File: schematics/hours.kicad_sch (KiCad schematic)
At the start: 53 parts, among them U27 74HC04, U28 74HC157, U29 74HC157, U30 74HC138, U32 74HC139

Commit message: 24-12 converter cleanup
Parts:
- removed D28, D29, D30, D31, D32, D33, D34, D35, D36: 1N4148, Diode_THT:D_DO-35_SOD27_P7.62mm_Horizontal, symbol Diode:1N4148
- removed R44: 1K, Package_DIP:DIP-16_W7.62mm, symbol Device:R
- removed R45, R46, R47: 10K, Package_DIP:DIP-16_W7.62mm, symbol Device:R
- removed unit 1 of U27
- added D46, D48, D53, D62: 1N4148, Diode_THT:D_DO-35_SOD27_P7.62mm_Horizontal, symbol Diode:1N4148
- added R53, R54: 4K7, Package_DIP:DIP-16_W7.62mm, symbol Device:R
- added U31: 74HC04, symbol 74xx:74HC04
- R48, R49, R50, R51, R52: value 10K -> 4K7
- U28, U29: value 74HC157 -> 74HC257
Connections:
- net +3V3: now also U29.3 (1B); no longer U30.6 (G1)
- net GND: now also U27.11, U28.15 (~{G}), U28.2 (1A), R53.2, R54.2; no longer U27.13, U30.5 (~{G}2B)
- net HI2: now also U27.13, D46.2 (A)
- net HI3: now also U30.4 (~{G}2A), D53.2 (A)
- net HI4: now also D48.2 (A)
- net HI5: now also U30.5 (~{G}2B), D62.2 (A)
- net at D37.2 (A), D45.2 (A), D47.2 (A)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: no longer U27.11
- net at U32.15 (2~{G}): now also U31.2
- net at U32.1 (1~{G}): now also U27.12, U30.6 (G1)
- net at U32.13 (2B): now also D46.1 (K), D48.1 (K), R53.1
- net at U27.10: no longer U29.3 (1B)
- new net: D53.1 (K), D62.1 (K), R54.1, U31.1
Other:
- note added: "12/24 mode switch"
- note added: "24 hour time in BCD"
- note added: "If leading digit is 0, setting upper bits 3 and 4 to '1' blanks instead of displaying it."
- note added: "Sets segment C of LED to make it "A" instead of "P"."
- note added: "always the same"
- moved on the sheet: C26, C27, C28, C29, C30, D37, D38, D41, D43, D45, D47, D49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

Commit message: added some PCB footprints
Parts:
- C20: renamed from C26; footprint Package_SO:SOIC-8_3.9x4.9mm_P1.27mm -> Capacitor_THT:C_Disc_D5.1mm_W3.2mm_P5.00mm
- C21: renamed from C27; footprint Package_SO:SOIC-8_3.9x4.9mm_P1.27mm -> Capacitor_THT:C_Disc_D5.1mm_W3.2mm_P5.00mm
- C22: renamed from C28; footprint Package_SO:SOIC-8_3.9x4.9mm_P1.27mm -> Capacitor_THT:C_Disc_D5.1mm_W3.2mm_P5.00mm
- C23: renamed from C29; footprint Package_SO:SOIC-8_3.9x4.9mm_P1.27mm -> Capacitor_THT:C_Disc_D5.1mm_W3.2mm_P5.00mm
- C24: renamed from C30; footprint Package_SO:SOIC-8_3.9x4.9mm_P1.27mm -> Capacitor_THT:C_Disc_D5.1mm_W3.2mm_P5.00mm
- R22: renamed from R53; footprint Package_DIP:DIP-16_W7.62mm -> Resistor_THT:R_Axial_DIN0207_L6.3mm_D2.5mm_P10.16mm_Horizontal
- R23: renamed from R54; footprint Package_DIP:DIP-16_W7.62mm -> Resistor_THT:R_Axial_DIN0207_L6.3mm_D2.5mm_P10.16mm_Horizontal
- R24: renamed from R52; footprint Package_DIP:DIP-16_W7.62mm -> Resistor_THT:R_Axial_DIN0207_L6.3mm_D2.5mm_P10.16mm_Horizontal
- R25: renamed from R48; footprint Package_DIP:DIP-16_W7.62mm -> Resistor_THT:R_Axial_DIN0207_L6.3mm_D2.5mm_P10.16mm_Horizontal
- R26: renamed from R49; footprint Package_DIP:DIP-16_W7.62mm -> Resistor_THT:R_Axial_DIN0207_L6.3mm_D2.5mm_P10.16mm_Horizontal
- R27: renamed from R50; footprint Package_DIP:DIP-16_W7.62mm -> Resistor_THT:R_Axial_DIN0207_L6.3mm_D2.5mm_P10.16mm_Horizontal
- R28: renamed from R51; footprint Package_DIP:DIP-16_W7.62mm -> Resistor_THT:R_Axial_DIN0207_L6.3mm_D2.5mm_P10.16mm_Horizontal
- U11: renamed from U27; footprint (none) -> Package_DIP:DIP-14_W7.62mm
- U11: renamed from U31; footprint (none) -> Package_DIP:DIP-14_W7.62mm
- U13: renamed from U30; footprint Package_TO_SOT_SMD:SOT-23-5 -> Package_DIP:DIP-16_W7.62mm
- U14: renamed from U28; footprint Filter:Filter_1411-5_1.4x1.1mm -> Package_DIP:DIP-16_W7.62mm
- U15: renamed from U29; footprint Filter:Filter_1411-5_1.4x1.1mm -> Package_DIP:DIP-16_W7.62mm
- renumbered D46 to D24, D48 to D25, D53 to D26, D62 to D27, D52 to D28, D51 to D29, D57 to D30, D58 to D31, D59 to D32, D60 to D33, D61 to D34, D37 to D35, D45 to D36, D47 to D37, D49 to D38, D72 to D39, D71 to D40, D74 to D41, D69 to D42, D55 to D43, D70 to D44, D75 to D45, D38 to D46, D41 to D47, D43 to D48, D50 to D49, D54 to D50, D56 to D51, D76 to D52, U32 to U12

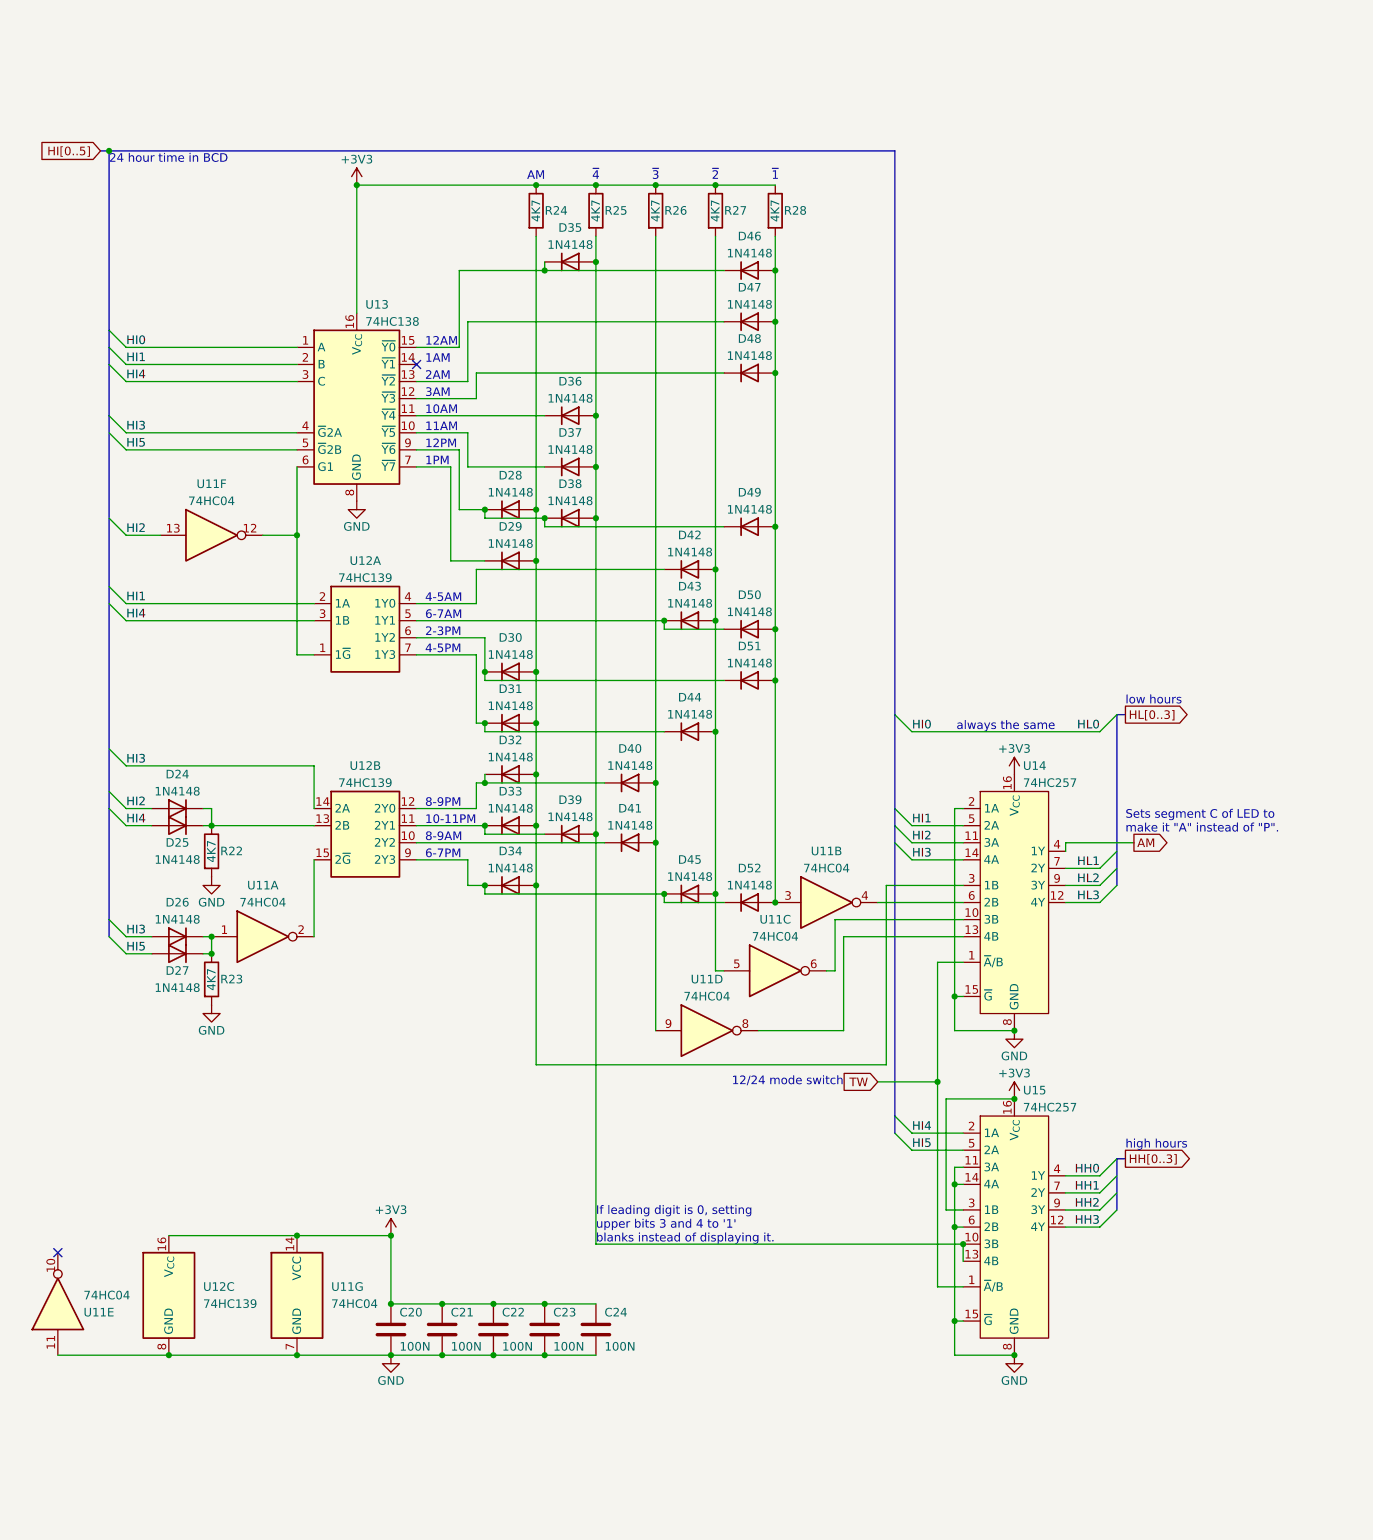
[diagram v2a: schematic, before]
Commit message: switched to PWM for LEDs
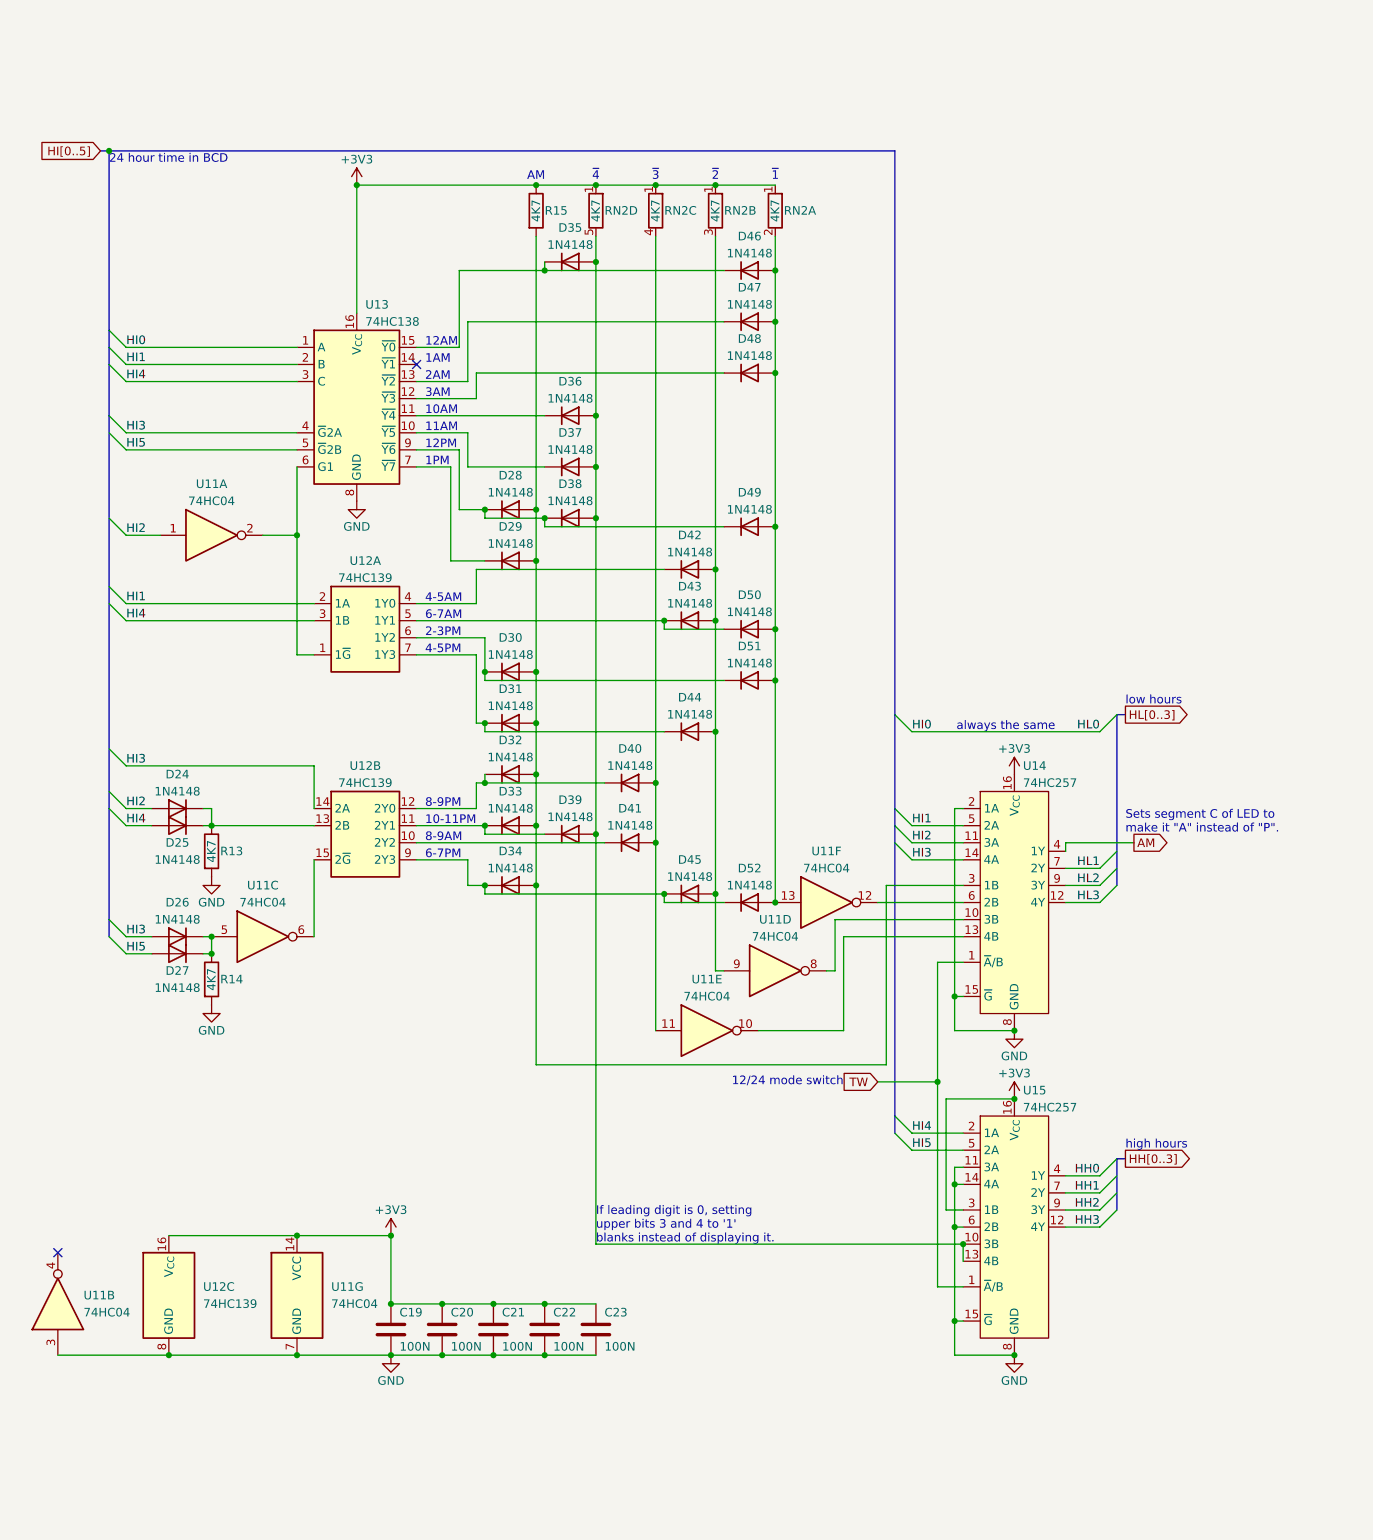
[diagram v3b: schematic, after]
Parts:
- removed R24, R25, R26, R27, R28: 4K7, Resistor_THT:R_Axial_DIN0207_L6.3mm_D2.5mm_P10.16mm_Horizontal, symbol Device:R
- added R15: 4K7, Resistor_THT:R_Axial_DIN0207_L6.3mm_D2.5mm_P7.62mm_Horizontal, symbol Device:R
- added RN2: 4K7, Resistor_THT:R_Array_SIP9, symbol Device:R_Network08_Split
- R13: renamed from R22; footprint Resistor_THT:R_Axial_DIN0207_L6.3mm_D2.5mm_P10.16mm_Horizontal -> Resistor_THT:R_Axial_DIN0207_L6.3mm_D2.5mm_P7.62mm_Horizontal
- R14: renamed from R23; footprint Resistor_THT:R_Axial_DIN0207_L6.3mm_D2.5mm_P10.16mm_Horizontal -> Resistor_THT:R_Axial_DIN0207_L6.3mm_D2.5mm_P7.62mm_Horizontal
- renumbered C20 to C19, C21 to C20, C22 to C21, C23 to C22, C24 to C23
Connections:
- net +3V3: now also R15.1, RN2.1 (R1), RN2.1 (R1), RN2.1 (R1), RN2.1 (R1)
- net GND: now also U11.3; no longer U11.11
- net HI2: now also U11.1; no longer U11.13
- net at D26.1 (K), D27.1 (K), R14.1: now also U11.5; no longer U11.1
- net at D42.2 (A), D43.2 (A), D44.2 (A)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: now also U11.9, RN2.3 (R2.2); no longer U11.5
- net at D35.2 (A), D36.2 (A), D37.2 (A)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: now also RN2.5 (R4.2)
- net at U12.1 (1~{G}), U13.6 (G1): now also U11.2; no longer U11.12
- net at U14.10 (3B): now also U11.8; no longer U11.6
- net at U14.13 (4B): now also U11.10; no longer U11.8
- net at D28.2 (A), D29.2 (A), D30.2 (A)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: now also R15.2
- net at U14.6 (2B): now also U11.12; no longer U11.4
- net at D46.2 (A), D47.2 (A), D48.2 (A)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: now also U11.13, RN2.2 (R1.2); no longer U11.3
- net at D40.2 (A), D41.2 (A): now also U11.11, RN2.4 (R3.2); no longer U11.9
- net at U12.15 (2~{G}): now also U11.6; no longer U11.2

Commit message: fiddled with transistors
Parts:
- renumbered C19 to C20, C20 to C21, C21 to C22, C22 to C23, C23 to C24, D24 to D23, D25 to D24, D26 to D25, D27 to D26, D28 to D27, D29 to D28, D30 to D29, D31 to D30, D32 to D31, D33 to D32, D34 to D33, D35 to D34, D36 to D35, D37 to D36, D38 to D37, D39 to D38, D40 to D39, D41 to D40, D42 to D41, D43 to D42, D44 to D43, D45 to D44, D46 to D45, D47 to D46, D48 to D47, D49 to D48, D50 to D49, D51 to D50, D52 to D51, R13 to R18, R14 to R19, R15 to R20

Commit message: preliminary PCB design
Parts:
- removed D23, D24, D25, D26: 1N4148, Diode_THT:D_DO-35_SOD27_P7.62mm_Horizontal, symbol Diode:1N4148
- removed R18, R19: 4K7, Resistor_THT:R_Axial_DIN0207_L6.3mm_D2.5mm_P7.62mm_Horizontal, symbol Device:R
- removed RN2: 4K7, Resistor_THT:R_Array_SIP9, symbol Device:R_Network08_Split
- added C33: 100N, bvclock:THT_Cap, symbol Device:C
- added RN2: 4K7, Resistor_THT:R_Array_SIP5, symbol Device:R_Network04_Split
- added U32: 74HC32, Package_DIP:DIP-14_W7.62mm, symbol 74xx:74LS32
- C20, C21, C22, C23, C24: footprint Capacitor_THT:C_Disc_D5.1mm_W3.2mm_P5.00mm -> bvclock:THT_Cap
- D27, D28, D29, D30, D31, D32, D33, D34, D35, D36, D37, D38, D39, D40, D41, D42, D43, D44, D45, D46, D47, D48, D49, D50, D51: footprint Diode_THT:D_DO-35_SOD27_P7.62mm_Horizontal -> bvclock:THT_D_Vertical
- R20: footprint Resistor_THT:R_Axial_DIN0207_L6.3mm_D2.5mm_P7.62mm_Horizontal -> bvclock:THT_R_Vertical
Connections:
- net +3V3: now also R20.2, C33.1, RN2.1 (R1), RN2.1 (R1), RN2.1 (R1), RN2.1 (R1), U32.14 (VCC); no longer R20.1
- net GND: now also C33.2, U32.1, U32.2, U32.7 (GND)
- net HI2: now also U32.4
- net HI3: now also U32.9
- net HI4: now also U32.5
- net HI5: now also U32.10
- net at U11.5: now also U32.8
- net at D41.2 (A), D42.2 (A), D43.2 (A)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: now also RN2.2 (R1.2)
- net at D34.2 (A), D35.2 (A), D36.2 (A)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: now also R20.1
- net at D39.2 (A), D40.2 (A), U11.11: now also RN2.3 (R2.2)
- net at D27.2 (A), D28.2 (A), D29.2 (A)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: now also RN2.5 (R4.2); no longer R20.2
- net at U12.13 (2B): now also U32.6
- net at D45.2 (A), D46.2 (A), D47.2 (A)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: now also RN2.4 (R3.2)
- no-connect marks 2 -> 3
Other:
- moved on the sheet: C20, C21, C22, C23, C24, U11B, U11C, U11G, U12C

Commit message: passes DRC
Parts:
- C20, C21, C22, C23, C24, C33: value 100N -> 100n
- R20, RN2: value 4K7 -> 4k7
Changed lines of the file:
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@@
 			)
 		)
-		(property "Value" "100N"
+		(property "Value" "100n"
 			(at 96.52 231.14 0)
 			(show_name no)
@@
 			)
 		)
-		(property "Value" "4K7"
+		(property "Value" "4k7"
 			(at 96.52 41.91 90)
 			(show_name no)
@@
 			)
 		)
-		(property "Value" "100N"
+		(property "Value" "100n"
 			(at 104.14 231.14 0)
 			(show_name no)
@@
 			)
 		)
-		(property "Value" "4K7"
+		(property "Value" "4k7"
 			(at 123.19 41.91 90)
 			(show_name no)
@@
 			)
 		)
-		(property "Value" "100N"
+		(property "Value" "100n"
 			(at 81.28 231.14 0)
 			(show_name no)
@@
 			)
 		)
-		(property "Value" "100N"
+		(property "Value" "100n"
 			(at 88.9 231.14 0)
 			(show_name no)
@@
 			)
 		)
-		(property "Value" "100N"
+		(property "Value" "100n"
 			(at 119.38 231.14 0)
 			(show_name no)
@@
 			)
 		)
-		(property "Value" "4K7"
+		(property "Value" "4k7"
 			(at 105.41 41.91 90)
 			(show_name no)
@@
 			)
 		)
-		(property "Value" "4K7"
+		(property "Value" "4k7"
 			(at 87.63 41.91 90)
 			(show_name no)
@@
 			)
 		)
-		(property "Value" "100N"
+		(property "Value" "100n"
 			(at 111.76 231.14 0)
 			(show_name no)
@@
 			)
 		)
-		(property "Value" "4K7"
+		(property "Value" "4k7"
 			(at 114.3 41.91 90)
 			(show_name no)
